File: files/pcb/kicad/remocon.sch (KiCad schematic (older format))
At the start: 0 parts

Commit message: 回路図更新
温度湿度センサ
大気圧センサ
輝度センサ
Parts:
- added S?: SENSOR, symbol SENSOR
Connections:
- new net +5V: S?.1 (VCC)
- new net GND: S?.2 (GND)
- new net out: S?.3 (OUT)
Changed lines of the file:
@@
 $Descr A4 11693 8268
 encoding utf-8
-Sheet 1 12
+Sheet 8 12
 Title ""
 Date "23 aug 2014"
@@
 Comment4 ""
 $EndDescr
+$Comp
+L SENSOR S?
+U 1 1 53F8FE49
+P 5800 4200
+F 0 "S?" H 5900 3950 39  0000 C CNN
+F 1 "SENSOR" H 5650 3950 39  0000 C CNN
+F 2 "" H 5500 4050 60  0000 C CNN
+F 3 "" H 5500 4050 60  0000 C CNN
+	1    5800 4200
+	1    0    0    -1
+$EndComp
+$Comp
+L GND #PWR?
+U 1 1 53F8FE58
+P 5800 4800
+F 0 "#PWR?" H 5800 4800 30  0001 C CNN
+F 1 "GND" H 5800 4730 30  0001 C CNN
+F 2 "" H 5800 4800 60  0000 C CNN
+F 3 "" H 5800 4800 60  0000 C CNN
+	1    5800 4800
+	1    0    0    -1
+$EndComp
+$Comp
+L +5V #PWR?
+U 1 1 53F8FE67
+P 5800 3550
+F 0 "#PWR?" H 5800 3640 20  0001 C CNN
+F 1 "+5V" H 5800 3640 30  0000 C CNN
+F 2 "" H 5800 3550 60  0000 C CNN
+F 3 "" H 5800 3550 60  0000 C CNN
+	1    5800 3550
+	1    0    0    -1
+$EndComp
+Text HLabel 6300 4200 2    60   Input ~ 0
+out
+Wire Wire Line
+	6250 4200 6300 4200
+Wire Wire Line
+	5800 3700 5800 3550
+Wire Wire Line
+	5800 4700 5800 4800
 $EndSCHEMATC

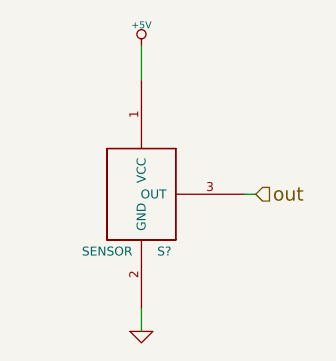
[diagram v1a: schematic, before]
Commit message: 回路図更新、DS1307対応
バスの接続が未
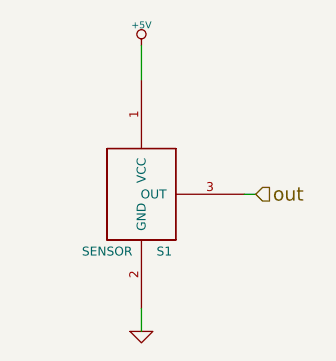
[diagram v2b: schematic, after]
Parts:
- gave numbers to parts that had none: 1
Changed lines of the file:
@@
 $Descr A4 11693 8268
 encoding utf-8
-Sheet 8 12
+Sheet 8 13
 Title ""
-Date "23 aug 2014"
+Date "24 aug 2014"
 Rev ""
 Comp ""
@@
 $EndDescr
 $Comp
-L SENSOR S?
+L SENSOR S1
 U 1 1 53F8FE49
 P 5800 4200
-F 0 "S?" H 5900 3950 39  0000 C CNN
+F 0 "S1" H 5900 3950 39  0000 C CNN
 F 1 "SENSOR" H 5650 3950 39  0000 C CNN
 F 2 "" H 5500 4050 60  0000 C CNN
@@
 $EndComp
 $Comp
-L GND #PWR?
+L GND #PWR48
 U 1 1 53F8FE58
 P 5800 4800
-F 0 "#PWR?" H 5800 4800 30  0001 C CNN
+F 0 "#PWR48" H 5800 4800 30  0001 C CNN
 F 1 "GND" H 5800 4730 30  0001 C CNN
 F 2 "" H 5800 4800 60  0000 C CNN
@@
 $EndComp
 $Comp
-L +5V #PWR?
+L +5V #PWR47
 U 1 1 53F8FE67
 P 5800 3550
-F 0 "#PWR?" H 5800 3640 20  0001 C CNN
+F 0 "#PWR47" H 5800 3640 20  0001 C CNN
 F 1 "+5V" H 5800 3640 30  0000 C CNN
 F 2 "" H 5800 3550 60  0000 C CNN

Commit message: 回路図ERC途中
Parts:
- renumbered S1 to U14
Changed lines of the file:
@@
 $Descr A4 11693 8268
 encoding utf-8
-Sheet 8 13
+Sheet 9 13
 Title ""
-Date "24 aug 2014"
+Date "25 aug 2014"
 Rev ""
 Comp ""
@@
 $EndDescr
 $Comp
-L SENSOR S1
+L SENSOR U14
 U 1 1 53F8FE49
 P 5800 4200
-F 0 "S1" H 5900 3950 39  0000 C CNN
+F 0 "U14" H 5900 3950 39  0000 C CNN
 F 1 "SENSOR" H 5650 3950 39  0000 C CNN
 F 2 "" H 5500 4050 60  0000 C CNN
@@
 $EndComp
 $Comp
-L GND #PWR48
+L GND #PWR047
 U 1 1 53F8FE58
 P 5800 4800
-F 0 "#PWR48" H 5800 4800 30  0001 C CNN
+F 0 "#PWR047" H 5800 4800 30  0001 C CNN
 F 1 "GND" H 5800 4730 30  0001 C CNN
 F 2 "" H 5800 4800 60  0000 C CNN
@@
 $EndComp
 $Comp
-L +5V #PWR47
+L +5V #PWR048
 U 1 1 53F8FE67
 P 5800 3550
-F 0 "#PWR47" H 5800 3640 20  0001 C CNN
+F 0 "#PWR048" H 5800 3640 20  0001 C CNN
 F 1 "+5V" H 5800 3640 30  0000 C CNN
 F 2 "" H 5800 3550 60  0000 C CNN

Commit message: 部品リスト・パッケージライブラリを更新
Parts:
- renumbered U14 to U13
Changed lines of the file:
@@
 $EndDescr
 $Comp
-L SENSOR U14
+L SENSOR U13
 U 1 1 53F8FE49
 P 5800 4200
-F 0 "U14" H 5900 3950 39  0000 C CNN
+F 0 "U13" H 5900 3950 39  0000 C CNN
 F 1 "SENSOR" H 5650 3950 39  0000 C CNN
 F 2 "" H 5500 4050 60  0000 C CNN
@@
 $EndComp
 $Comp
-L GND #PWR055
+L GND #PWR058
 U 1 1 53F8FE58
 P 5800 4800
-F 0 "#PWR055" H 5800 4800 30  0001 C CNN
+F 0 "#PWR058" H 5800 4800 30  0001 C CNN
 F 1 "GND" H 5800 4730 30  0001 C CNN
 F 2 "" H 5800 4800 60  0000 C CNN
@@
 $EndComp
 $Comp
-L +5V #PWR056
+L +5V #PWR059
 U 1 1 53F8FE67
 P 5800 3550
-F 0 "#PWR056" H 5800 3640 20  0001 C CNN
+F 0 "#PWR059" H 5800 3640 20  0001 C CNN
 F 1 "+5V" H 5800 3640 30  0000 C CNN
 F 2 "" H 5800 3550 60  0000 C CNN

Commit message: 部品リスト完了、PCBに部品を配置
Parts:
- added C16: 0.1u, ~, symbol C
- U13: value SENSOR -> remocon
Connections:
- net +5V: now also C16.1
- net GND: now also C16.2
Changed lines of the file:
@@
 Sheet 9 13
 Title ""
-Date "26 aug 2014"
+Date "28 aug 2014"
 Rev ""
 Comp ""
@@
 P 5800 4200
 F 0 "U13" H 5900 3950 39  0000 C CNN
-F 1 "SENSOR" H 5650 3950 39  0000 C CNN
+F 1 "remocon" H 5650 3950 39  0000 C CNN
 F 2 "" H 5500 4050 60  0000 C CNN
 F 3 "" H 5500 4050 60  0000 C CNN
@@
 Wire Wire Line
 	5800 4700 5800 4800
+$Comp
+L C C16
+U 1 1 53FF6073
+P 5350 4150
+F 0 "C16" H 5350 4250 40  0000 L CNN
+F 1 "0.1u" H 5356 4065 40  0000 L CNN
+F 2 "~" H 5388 4000 30  0000 C CNN
+F 3 "~" H 5350 4150 60  0000 C CNN
+	1    5350 4150
+	1    0    0    -1
+$EndComp
+Wire Wire Line
+	5800 3700 5350 3700
+Wire Wire Line
+	5350 3700 5350 3950
+Wire Wire Line
+	5350 4350 5350 4700
+Wire Wire Line
+	5350 4700 5800 4700
 $EndSCHEMATC
